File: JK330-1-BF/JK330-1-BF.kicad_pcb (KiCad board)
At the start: 2 copper layers, 141 parts, among them K1 CONN_2, K10 COLONETTE, K11 CONN_3, K2 CONN_2, K3 CONN_3, K4 CONN_2, K5 COLONETTE, K6 COLONETTE, K7 COLONETTE, K8 COLONETTE, K9 COLONETTE, P1 U.FL, P2 U.FL, P3 U.FL, P4 CONN_5, P5 HE10-16, P6 CONN_6, P7 CAVALIER, P8 CAVALIER, Q1 BC847, Q2 BC847, Q3 BSP250, Q4 BC847, Q5 BSP250, U1 MF10, U10 TDA2003, U2 74HC4059, U3 74HC377, U4 74HC74, U5 16Mhz, U6 MC33172, U7 MF10, U8 74HC4059, U9 74HC377

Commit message: Fin Routage PCb V0-10
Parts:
- removed K4: CONN_2, KK-2
- C1, C10, C18, C2, C20, C28, C29, C33, C34, C35, C8: footprint SM1812 -> SM2112L
- C25: footprint SM2010 -> SM2112L
- C31: value 100U -> 100u
- moved C25 5.14 mm to (220.2, 140.0)
- moved C20 3.95 mm to (188.2, 141.2)
- moved R4 3.94 mm to (127.3, 115.6)
- moved R45 3.81 mm to (229.4, 140.7)
- moved C30 3.56 mm to (229.4, 137.7)
- moved Q2 3.53 mm to (130.3, 165.4)
- moved R30 3.53 mm to (160.3, 133.9)
- moved R32 3.53 mm to (160.3, 135.6)
- moved R34 3.53 mm to (160.3, 137.4)
- moved C29 2.81 mm to (227.3, 132.8)
- moved C26 2.55 mm to (219.5, 135.6)
- moved R51 2.29 mm to (124.7, 167.4)
- moved C28 2.18 mm to (193.5, 129.5)
- moved Q4 2.17 mm to (129.3, 156.5)
- moved R50 2.03 mm to (124.7, 169.2)
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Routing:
- net /MIC/+12VRX: track 71.0 -> 86.9 mm
- net GND: track 756.6 -> 743.0 mm, vias 21 -> 24
- net /BD7: track 113.9 -> 123.1 mm
- net +12V: track 276.6 -> 269.9 mm
- net +3.3V: track 182.3 -> 186.9 mm
- net /MIC/AFE: track 3.30 -> 7.73 mm
- net /HP/BFIN: track 7.62 -> 12.1 mm
- net N-0000047: track 42.1 -> 37.7 mm
- net N-0000036: track 23.6 -> 27.3 mm, vias 0 -> 2
- net /MIC/BFE: track 17.6 -> 20.6 mm
- net +5VA: track 168.4 -> 171.3 mm
- net N-0000077: track 4.22 -> 6.95 mm
- net N-00000100: track 40.3 -> 42.8 mm
- net /Filtre Passe Bas/CSFPB: track 79.2 -> 76.8 mm
- net /HP/HP1: track 117.4 -> 119.8 mm
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- added copper zone on B.Cu, net GND
- added copper zone on F.Cu, net GND
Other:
- board text added: "+12V +5VD +5VA -5VA +3.3V"
- board text added: "9MHZ"
- board text added: "AUDIO LEVEL"
- board text added: "FILTER CONTROL"
- board text added: "IN OL 9MHZ"
- board text added: "JK330-1-BF V0-10 F4DEB 2013"
- board text added: "LINE OUT"
- board text added: "MICRO"
- board text added: "POWER"
- board text added: "RX"
- board text added: "RX/TX CONTROL"
- board text added: "TX"

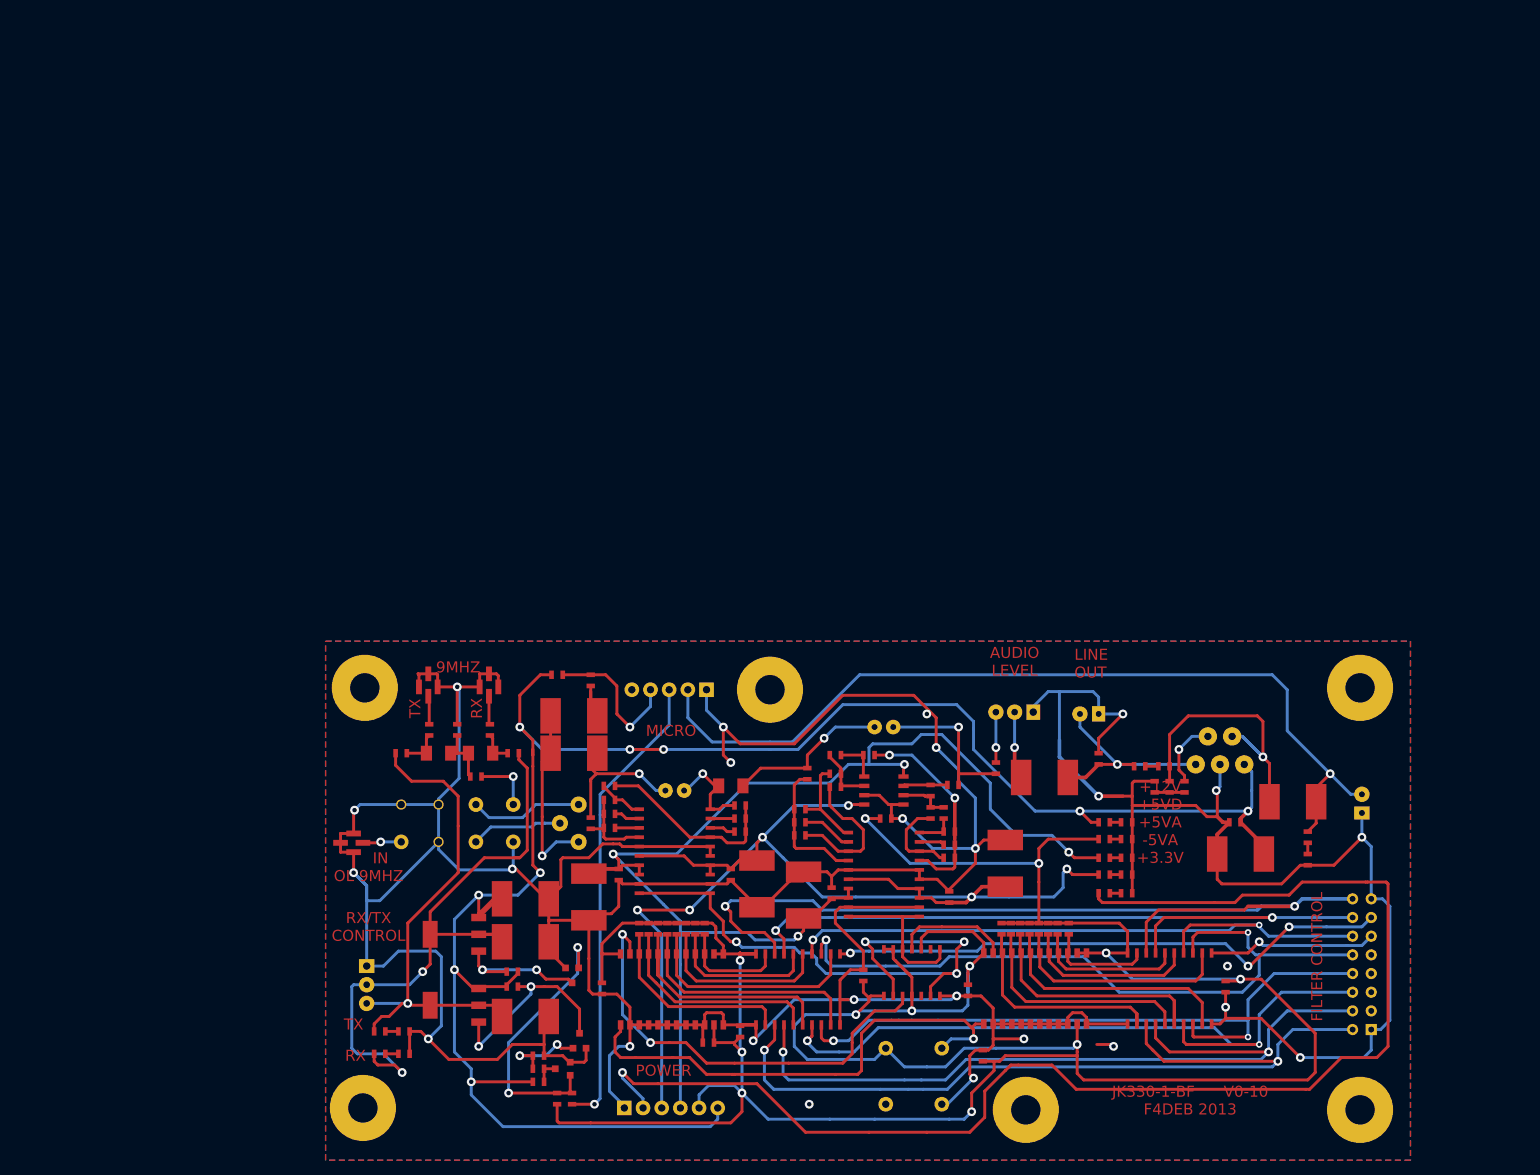
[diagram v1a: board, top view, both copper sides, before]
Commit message: LED CMS X4 12V
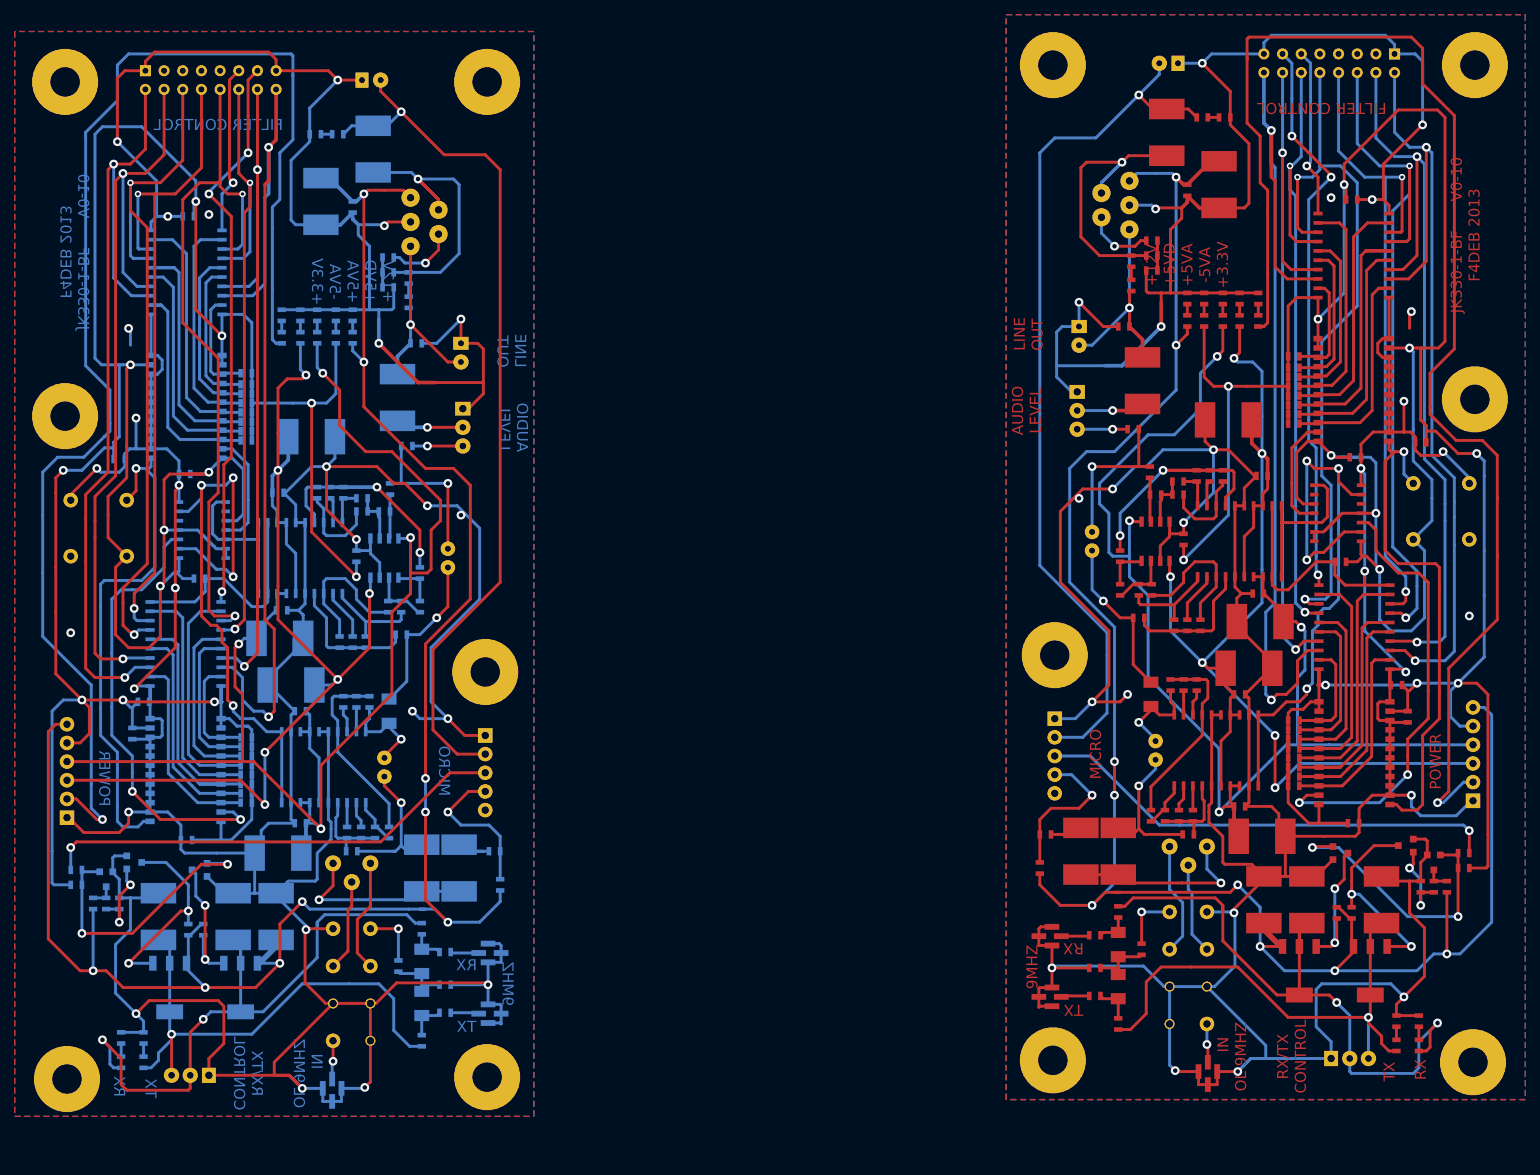
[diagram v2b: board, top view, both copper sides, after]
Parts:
- added C1: 10U, SM2112L, B.Cu at (108.8, 141.9)
- added C10: 10U, SM2112L, B.Cu at (91.1, 117.0)
- added C11: 100n, SM0603_Capa, B.Cu at (92.3, 120.5)
- added C12: 100n, SM0603_Capa, B.Cu at (69.5, 123.6)
- added C13: C, SM0603_Capa, B.Cu at (76.8, 138.0)
- added C14: 100n, SM0603_Capa, B.Cu at (71.0, 119.3)
- added C15: C, SM0603_Capa, B.Cu at (78.6, 102.5)
- added C16: 100n, SM0603_Capa, B.Cu at (67.7, 86.2)
- added C17: C, SM0603_Capa, B.Cu at (106.8, 84.5)
- added C18: CP, SM2112L, B.Cu at (89.5, 110.6)
- added C19: 100n, SM0603_Capa, B.Cu at (89.8, 106.8)
- added C2: 10U, SM2112L, B.Cu at (113.9, 141.9)
- added C20: CP, SM2112L, B.Cu at (93.9, 83.2)
- added C21: 100n, SM0603_Capa, B.Cu at (89.3, 90.8)
- added C22: 100n, SM0603_Capa, B.Cu at (99.9, 99.4)
- added C23: 100n, SM0603_Capa, B.Cu at (76.6, 88.3)
- added C24: 100n, SM0603_Capa, B.Cu at (77.1, 53.2)
- added C25: 1000U, SM2112L, B.Cu at (95.1, 51.2)
- added C26: 100n, SM0603_Capa, B.Cu at (99.4, 51.9)
- added C27: 470p, SM0603_Capa, B.Cu at (108.1, 70.5)
- added C28: 15n, SM2112L, B.Cu at (105.5, 77.9)
- added C29: 470U, SM2112L, B.Cu at (102.2, 44.1)
- added C3: 1n, SM0603_Capa, B.Cu at (112.0, 161.5)
- added C30: 100n, SM0603_Capa, B.Cu at (97.4, 42.0)
- added C31: 100u, SM0603_Capa, B.Cu at (104.3, 58.8)
- added C32: NC, SM0603_Capa, B.Cu at (107.1, 64.9)
- added C33: CP, SM2112L, B.Cu at (73.0, 148.5)
- added C34: CP, SM2112L, B.Cu at (89.0, 148.5)
- added C35: CP, SM2112L, B.Cu at (83.2, 148.5)
- added C4: 1n, SM0603_Capa, B.Cu at (105.7, 155.2)
- added C5: 1n, SM0603_Capa, B.Cu at (112.0, 153.3)
- added C6: C, SM0603_Capa, B.Cu at (118.7, 139.6)
- added C7: 1U, SM1206, B.Cu at (104.4, 120.5)
- added C8: 10U, SM2112L, B.Cu at (89.3, 139.8)
- added C9: 100n, SM0603_Capa, B.Cu at (92.3, 135.8)
- added D1: MA4P1250, SM1206, B.Cu at (108.8, 160.3)
- added D2: MA4P1250, SM1206, B.Cu at (108.8, 154.6)
- added D3: LED, SM0603, B.Cu at (99.4, 69.7)
- added D4: LED, SM0603, B.Cu at (97.2, 69.7)
- added D5: LED, SM0603, B.Cu at (94.6, 69.7)
- added D6: LED, SM0603, B.Cu at (92.3, 69.7)
- added D7: LED, SM0603, B.Cu at (89.8, 69.7)
- added D8: LED, SM0603, B.Cu at (71.0, 168.3)
- added D9: LED, SM0603, B.Cu at (67.9, 168.3)
- added K1: CONN_2, KK-2, B.Cu at (114.2, 73.0)
- added K10: COLONETTE, COLONETTE, B.Cu at (117.5, 115.2)
- added K11: CONN_3, KK-3, B.Cu at (114.4, 84.5)
- added K2: CONN_2, KK-2, B.Cu at (103.3, 34.7)
- added K3: CONN_3, KK-3, B.Cu at (74.8, 170.1)
- added K5: COLONETTE, COLONETTE, B.Cu at (117.7, 34.9)
- added K6: COLONETTE, COLONETTE, B.Cu at (60.3, 34.9)
- added K7: COLONETTE, COLONETTE, B.Cu at (60.6, 170.6)
- added K8: COLONETTE, COLONETTE, B.Cu at (60.3, 80.4)
- added K9: COLONETTE, COLONETTE, B.Cu at (117.7, 170.3)
- added MX1: SBL-1, SBL1, B.Cu at (99.3, 157.7)
- added P1: U.FL, UFL, B.Cu at (117.1, 160.9)
- added P2: U.FL, UFL, B.Cu at (117.1, 152.7)
- added P3: U.FL, UFL, B.Cu at (97.4, 171.1)
- added P4: CONN_5, KK-5, B.Cu at (117.5, 131.4)
- added P5: HE10-16, he10-16d, B.Cu at (80.1, 34.7)
- added P6: CONN_6, KK-6, B.Cu at (60.6, 128.7)
- added P7: CAVALIER, CAVALIER, B.Cu at (103.8, 129.4)
- added P8: CAVALIER, CAVALIER, B.Cu at (112.4, 101.0)
- added Q1: BC847, SOT23EBC, B.Cu at (65.9, 143.4)
- added Q2: BC847, SOT23EBC, B.Cu at (69.7, 141.1)
- added Q3: BSP250, SOT223, B.Cu at (74.5, 158.1)
- added Q4: BC847, SOT23EBC, B.Cu at (78.6, 142.1)
- added Q5: BSP250, SOT223, B.Cu at (84.2, 158.1)
- added R1: 1k, SM0603_Resistor, B.Cu at (108.8, 165.4)
- added R10: 10k, SM0603_Resistor, B.Cu at (99.9, 119.3)
- added R11: 39k//39k, SM0603_Resistor, B.Cu at (98.7, 137.0)
- added R12: 39k//39k, SM0603_Resistor, B.Cu at (98.2, 119.3)
- added R13: 10k, SM0603_Resistor, B.Cu at (99.3, 139.6)
- added R14: 10k, SM0603_Resistor, B.Cu at (85.0, 133.0)
- added R15: 10k, SM0603_Resistor, B.Cu at (85.0, 131.7)
- added R16: 10k, SM0603_Resistor, B.Cu at (85.0, 130.4)
- added R17: 10k, SM0603_Resistor, B.Cu at (85.0, 129.2)
- added R18: 10k, SM0603_Resistor, B.Cu at (85.0, 127.9)
- added R19: 10k, SM0603_Resistor, B.Cu at (85.0, 126.6)
- added R2: 1k, SM0603_Resistor, B.Cu at (112.0, 157.7)
- added R20: 10k, SM0603_Resistor, B.Cu at (85.0, 125.3)
- added R21: 10k, SM0603_Resistor, B.Cu at (85.0, 124.1)
- added R22: 11.5k, SM0603_Resistor, B.Cu at (104.3, 106.3)
- added R23: 11.5k, SM0603_Resistor, B.Cu at (108.6, 106.3)
- added R24: 11.5k, SM0603_Resistor, B.Cu at (106.0, 106.3)
- added R25: 11.5k, SM0603_Resistor, B.Cu at (108.6, 101.7)
- added R26: 11.5k, SM0603_Resistor, B.Cu at (100.7, 93.3)
- added R27: 11k5, SM0603_Resistor, B.Cu at (103.8, 93.3)
- added R28: 11k5, SM0603_Resistor, B.Cu at (100.7, 91.6)
- added R29: R, SM0603_Resistor, B.Cu at (104.5, 90.3)
- added R3: 1k, SM0603_Resistor, B.Cu at (108.8, 150.1)
- added R30: 11.5k, SM0603_Resistor, B.Cu at (101.2, 111.1)
- added R31: 11.5k, SM0603_Resistor, B.Cu at (98.2, 90.8)
- added R32: 100k, SM0603_Resistor, B.Cu at (99.4, 111.1)
- added R33: 100k, SM0603_Resistor, B.Cu at (96.4, 90.8)
- added R34: 11.5k, SM0603_Resistor, B.Cu at (97.7, 111.1)
- added R35: 11.5k, SM0603_Resistor, B.Cu at (94.6, 90.8)
- added R36: 11.5k, SM0603_Resistor, B.Cu at (106.0, 110.1)
- added R37: R, SM0603_Resistor, B.Cu at (85.0, 83.7)
- added R38: R, SM0603_Resistor, B.Cu at (85.0, 82.4)
- added R39: R, SM0603_Resistor, B.Cu at (85.0, 81.2)
- added R4: R, SM0603_Resistor, B.Cu at (119.5, 144.1)
- added R40: R, SM0603_Resistor, B.Cu at (85.0, 79.9)
- added R41: R, SM0603_Resistor, B.Cu at (85.0, 78.6)
- added R42: R, SM0603_Resistor, B.Cu at (85.0, 77.3)
- added R43: R, SM0603_Resistor, B.Cu at (85.0, 76.1)
- added R44: R, SM0603_Resistor, B.Cu at (85.0, 74.5)
- added R45: 1, SM0603_Resistor, B.Cu at (94.4, 42.0)
- added R46: 10, SM0603_Resistor, B.Cu at (104.3, 62.9)
- added R47: 470, SM0603_Resistor, B.Cu at (104.3, 60.8)
- added R48: NC, SM0603_Resistor, B.Cu at (107.1, 61.6)
- added R49: R, SM0603_Resistor, B.Cu at (64.1, 146.7)
- added R5: R, SM0603_Resistor, B.Cu at (61.8, 144.1)
- added R50: R, SM0603_Resistor, B.Cu at (65.9, 146.7)
- added R51: R, SM0603_Resistor, B.Cu at (67.7, 146.7)
- added R52: R, SM0603_Resistor, B.Cu at (77.1, 150.2)
- added R53: R, SM0603_Resistor, B.Cu at (61.8, 142.1)
- added R54: R, SM0603_Resistor, B.Cu at (79.1, 150.2)
- added R55: 1k, SM0603_Resistor, B.Cu at (99.4, 66.7)
- added R56: 1k, SM0603_Resistor, B.Cu at (97.2, 66.7)
- added R57: 1k, SM0603_Resistor, B.Cu at (94.6, 66.7)
- added R58: 1k, SM0603_Resistor, B.Cu at (92.3, 66.7)
- added R59: 1k, SM0603_Resistor, B.Cu at (89.8, 66.7)
- added R6: 10k, SM0603_Resistor, B.Cu at (104.4, 137.0)
- added R60: 1k, SM0603_Resistor, B.Cu at (71.0, 165.0)
- added R61: 1k, SM0603_Resistor, B.Cu at (67.9, 165.0)
- added R7: 10k, SM0603_Resistor, B.Cu at (102.5, 137.0)
- added R8: 10k, SM0603_Resistor, B.Cu at (101.7, 119.3)
- added R9: 10k, SM0603_Resistor, B.Cu at (100.6, 137.0)
- added RVAR1: 100, POT_10T_T93YB, B.Cu at (101.9, 141.2)
- added U1: MF10, SO20L, B.Cu at (95.5, 128.1)
- added U10: TDA2003, TDA2003V, B.Cu at (111.1, 54.0)
- added U2: 74HC4059, SO24E, B.Cu at (76.7, 128.5)
- added U3: 74HC377, SO20L, B.Cu at (76.7, 111.4)
- added U4: 74HC74, SO14N, B.Cu at (79.1, 95.9)
- added U5: 16Mhz, XTAL_QUAD, B.Cu at (64.9, 95.6)
- added U6: MC33172, SO8E, B.Cu at (103.8, 99.7)
- added U7: MF10, SO20L, B.Cu at (92.3, 99.7)
- added U8: 74HC4059, SO24E, B.Cu at (76.8, 79.1)
- added U9: 74HC377, SO20L, B.Cu at (76.8, 60.8)
- moved K7 151.1 mm to (251.8, 168.3), turned to 270 degrees
- moved K6 143.0 mm to (252.1, 32.6), turned to 90 degrees
- moved D9 141.4 mm to (244.5, 166.0), turned to 90 degrees
- moved D8 138.3 mm to (241.4, 166.0), turned to 90 degrees
- moved R61 138.1 mm to (244.5, 162.7), turned to 90 degrees
- moved K3 136.5 mm to (237.6, 167.8), turned to 180 degrees
- moved R60 135.0 mm to (241.4, 162.7), turned to 90 degrees
- moved R5 127.2 mm to (250.6, 141.9), turned to 180 degrees
- moved R49 126.4 mm to (248.3, 144.4), turned to 90 degrees
- moved R53 125.8 mm to (250.6, 139.8), turned to 180 degrees
- moved Q3 124.7 mm to (237.9, 155.8), turned to 180 degrees
- moved R50 124.3 mm to (246.5, 144.4), turned to 270 degrees
- moved P5 122.6 mm to (232.3, 32.4), turned to 180 degrees
- moved R51 122.2 mm to (244.7, 144.4), turned to 90 degrees
- moved Q1 121.8 mm to (246.5, 141.1), turned to 0 degrees
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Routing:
- net GND: track 743.0 -> 1481.2 mm, vias 24 -> 44
- net +5VD: track 431.5 -> 863.0 mm, vias 12 -> 24
- net +12V: track 269.9 -> 539.7 mm, vias 9 -> 18
- net +3.3V: track 186.9 -> 373.7 mm, vias 1 -> 2
- net +5VA: track 171.3 -> 342.6 mm, vias 4 -> 8
- net -5VA: track 163.5 -> 327.1 mm, vias 6 -> 12
- net /BD7: track 123.1 -> 246.3 mm, vias 2 -> 4
- net /HP/HP1: track 119.8 -> 239.6 mm, vias 1 -> 2
- net /BD0: track 114.9 -> 229.8 mm, vias 2 -> 4
- net /BD1: track 108.3 -> 216.6 mm, vias 2 -> 4
- net /BD6: track 102.9 -> 205.8 mm, vias 2 -> 4
- net /BD2: track 97.9 -> 195.7 mm, vias 2 -> 4
- net /BD4: track 97.1 -> 194.1 mm, vias 2 -> 4
- net /BD3: track 91.1 -> 182.2 mm, vias 2 -> 4
- net /BD5: track 90.6 -> 181.1 mm, vias 2 -> 4
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
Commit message: Ajout carte power
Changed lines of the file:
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@@
   (layers
     (15 Dessus.Cu signal)
-    (0 Dessous.Cu signal)
+    (0 Dessous.Cu signal hide)
     (16 Dessous.Adhes user)
     (17 Dessus.Adhes user)
@@
     (pad_to_mask_clearance 0.2)
     (aux_axis_origin 0 0)
-    (visible_elements 7FFFFFFF)
+    (visible_elements 7FFFFBFF)
     (pcbplotparams
       (layerselection 3178497)
@@
   (module UFL (layer Dessus.Cu)
     (at 195.326 150.368 270)
-    (fp_text reference P2 (at -1.27 -5.08 270) (layer Dessus.SilkS)
+    (fp_text reference P2 (at -1.778 2.286 270) (layer Dessus.SilkS)
       (effects (font (size 1.524 1.524) (thickness 0.3048)))
     )
-    (fp_text value U.FL (at 0 -7.62 270) (layer Dessus.SilkS)
+    (fp_text value U.FL (at -1.778 4.826 270) (layer Dessus.SilkS)
       (effects (font (size 1.524 1.524) (thickness 0.3048)))
     )
@@
   (module UFL (layer Dessus.Cu)
     (at 195.326 158.623 270)
-    (fp_text reference P1 (at -1.27 -5.08 270) (layer Dessus.SilkS)
+    (fp_text reference P1 (at 2.667 2.286 270) (layer Dessus.SilkS)
       (effects (font (size 1.524 1.524) (thickness 0.3048)))
     )
-    (fp_text value U.FL (at 0 -7.62 270) (layer Dessus.SilkS)
+    (fp_text value U.FL (at 2.667 4.826 270) (layer Dessus.SilkS)
       (effects (font (size 1.524 1.524) (thickness 0.3048)))
     )
@@
     (effects (font (size 1.5 1.5) (thickness 0.3)) (justify mirror))
   )
-  (gr_text TX (at 114.935 163.449 360) (layer Dessous.Cu)
+  (gr_text TX (at 114.935 163.449) (layer Dessous.Cu)
     (effects (font (size 1.5 1.5) (thickness 0.3)) (justify mirror))
   )
-  (gr_text RX (at 114.935 155.067 360) (layer Dessous.Cu)
+  (gr_text RX (at 114.935 155.067) (layer Dessous.Cu)
     (effects (font (size 1.5 1.5) (thickness 0.3)) (justify mirror))
   )
@@
     (effects (font (size 1.5 1.5) (thickness 0.3)) (justify left mirror))
   )
-  (gr_text "FILTER CONTROL" (at 81.153 40.767 360) (layer Dessous.Cu)
+  (gr_text "FILTER CONTROL" (at 81.153 40.767) (layer Dessous.Cu)
     (effects (font (size 1.5 1.5) (thickness 0.3)) (justify mirror))
   )
